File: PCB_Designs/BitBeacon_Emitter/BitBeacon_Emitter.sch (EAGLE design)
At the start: 9 parts, among them IC1 AD8607RM, IC2 AD8603UJ, Q1 TIP120

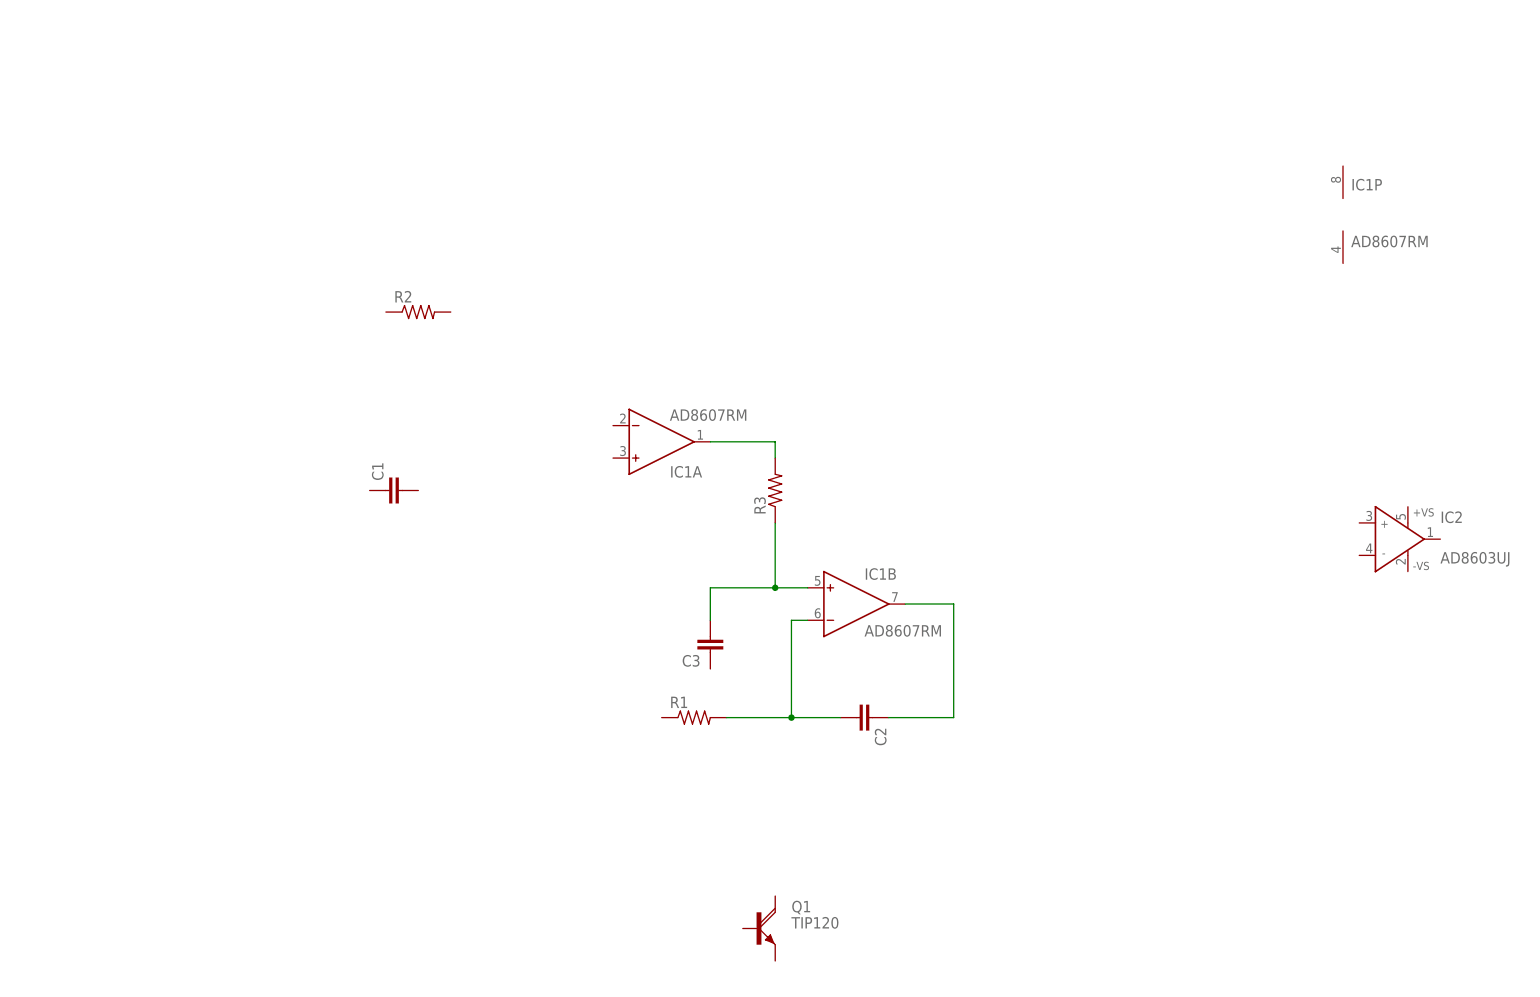
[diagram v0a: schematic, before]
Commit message: updating pcb files for emitter circuit
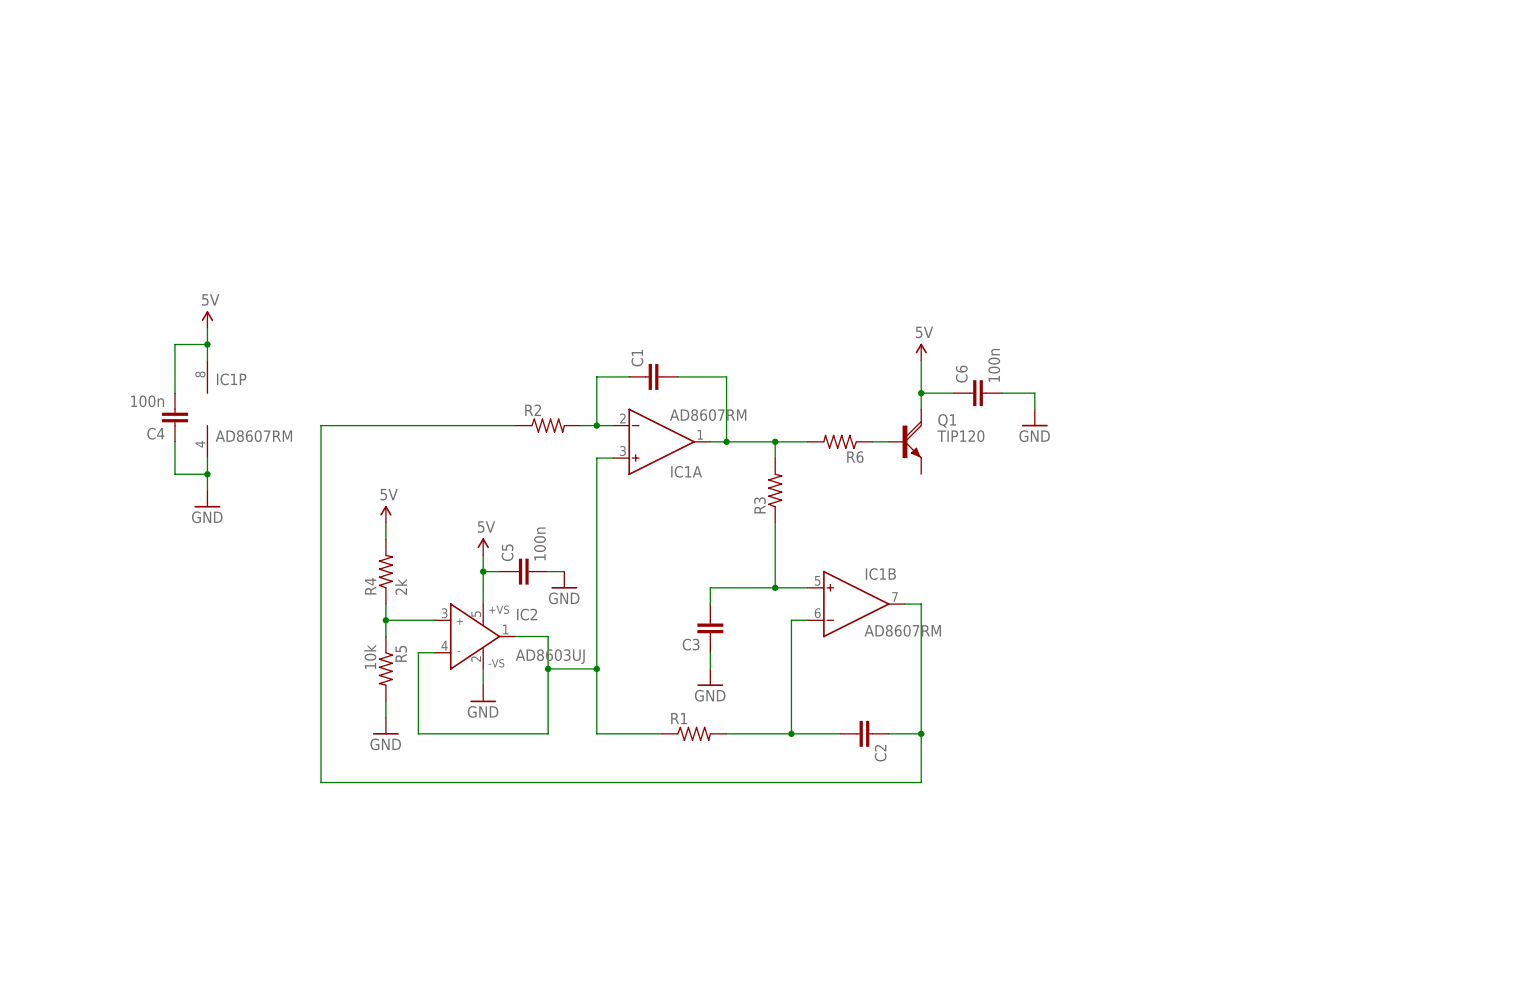
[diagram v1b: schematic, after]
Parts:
- added C4, C5, C6: 100n, resistor:C-EUC0402
- added R4: 2k, resistor:R-US_R0402
- added R5: 10k, resistor:R-US_R0402
- added R6: (no value), resistor:R-US_R0402
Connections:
- new net 5V: C4.2, C5.1, C6.1, IC1P.V+, IC2.+VS, Q1.C, R4.2
- new net GND: C3.1, C4.1, C5.2, C6.2, IC1P.V-, IC2.-VS, R5.2
- new net N$12: Q1.B, R6.1
- new net N$3: C1.1, IC1A.IN-, R2.2
- new net N$6: IC1A.IN+, IC2.IN-, IC2.OUT, R1.1
- new net N$7: IC2.IN+, R4.1, R5.1
- net N$1: now also C1.2, R6.2
- net N$4: now also R2.1
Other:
- moved on the sheet: C1, C2, C3, IC1P, IC2, Q1, R1, R2

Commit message: finished PCB design for Bit Beacon Emitter circuit and added datsheets for the LEDs that I think would work well.
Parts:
- removed Q1: TIP120, transistor-power:TIP120
- added JP1, JP2: M01NOSILK-KIT, SparkFun-Connectors:M01NOSILK-KIT
- added LED1, LED2, LED3: LED, Orlando:LED
- added LOGO1: OSHW-LOGOS, SparkFun-Aesthetics:OSHW-LOGOS
- added Q2: (no value), SparkFun-DiscreteSemi:TRANSISTOR_NPN2N3904
- added U$1: BATT-CONNECT, OrlandoRonMod:BATT-CONNECT
- C6: value 100n -> (none)
- R4: value 2k -> 5.1k
- renumbered IC1 to FGEN, IC2 to VREF
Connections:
- removed net N$1: C1.2, FGENA.OUT, R3.2, R6.2
- removed net N$12: Q1.B, R6.1
- removed net N$4: C2.1, FGENB.OUT, R2.1
- new net COSINE: C2.1, FGENB.OUT, JP2.1, R2.1
- new net N$8: LED1.C, LED2.C, LED3.C, Q2.C
- new net N$9: Q2.B, R6.1
- new net SINE: C1.2, FGENA.OUT, JP1.1, R3.2, R6.2
- net 5V: now also LED1.A, LED2.A, LED3.A, U$1G$2.TP; no longer Q1.C
- net GND: now also Q2.E, U$1G$1.TP
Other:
- note added: "Orlando S. Hoilett Bit Beacon Signal V.1.0 Calvary Eng, IICEPD Description: Sine wave generator circuit that drives a transistor to drive a few IR LEDs"
- note added: "Sources: Jean-Claude Wippler. "Generating a sine wave." <http://jeelabs.org/2012/05/18/generating-a-sine-wave/> Accessed: October 2015"
- moved on the sheet: C6, R6

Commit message: updated Bit emitter PCB design with resistor and capacitor values. Added a bill of materials for BitBeacon and BitBeacon_Emitter
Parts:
- C1, C2, C3: value (none) -> 1n
- C6: value (none) -> 100n
- R1, R2, R3: value (none) -> 22k
- R4: value 5.1k -> 22k
- R5: value 10k -> 22k
- R6: value (none) -> 100-400
- renumbered U$1 to BATTERY
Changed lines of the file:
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@@
 <?xml version="1.0" encoding="utf-8"?>
 <!DOCTYPE eagle SYSTEM "eagle.dtd">
-<eagle version="7.4.0">
+<eagle version="7.3.0">
 <drawing>
 <settings>
@@
 <part name="FGEN" library="analog-devices" deviceset="AD8607" device="RM" value=""/>
 <part name="VREF" library="analog-devices" deviceset="AD8603" device="UJ" value=""/>
-<part name="R1" library="resistor" deviceset="R-US_" device="R0402"/>
-<part name="R2" library="resistor" deviceset="R-US_" device="R0402"/>
-<part name="R3" library="resistor" deviceset="R-US_" device="R0402"/>
-<part name="C1" library="resistor" deviceset="C-EU" device="C0402"/>
-<part name="C2" library="resistor" deviceset="C-EU" device="C0402"/>
-<part name="C3" library="resistor" deviceset="C-EU" device="C0402"/>
+<part name="R1" library="resistor" deviceset="R-US_" device="R0402" value="22k"/>
+<part name="R2" library="resistor" deviceset="R-US_" device="R0402" value="22k"/>
+<part name="R3" library="resistor" deviceset="R-US_" device="R0402" value="22k"/>
+<part name="C1" library="resistor" deviceset="C-EU" device="C0402" value="1n"/>
+<part name="C2" library="resistor" deviceset="C-EU" device="C0402" value="1n"/>
+<part name="C3" library="resistor" deviceset="C-EU" device="C0402" value="1n"/>
 <part name="GND1" library="SparkFun-Aesthetics" deviceset="GND" device=""/>
-<part name="R4" library="resistor" deviceset="R-US_" device="R0402" value="5.1k"/>
-<part name="R5" library="resistor" deviceset="R-US_" device="R0402" value="10k"/>
+<part name="R4" library="resistor" deviceset="R-US_" device="R0402" value="22k"/>
+<part name="R5" library="resistor" deviceset="R-US_" device="R0402" value="22k"/>
 <part name="GND2" library="SparkFun-Aesthetics" deviceset="GND" device=""/>
 <part name="GND3" library="SparkFun-Aesthetics" deviceset="GND" device=""/>
@@
 <part name="C5" library="resistor" deviceset="C-EU" device="C0402" value="100n"/>
 <part name="GND5" library="SparkFun-Aesthetics" deviceset="GND" device=""/>
-<part name="R6" library="resistor" deviceset="R-US_" device="R0402"/>
+<part name="R6" library="resistor" deviceset="R-US_" device="R0402" value="100-400"/>
 <part name="SUPPLY4" library="SparkFun-Aesthetics" deviceset="5V" device=""/>
 <part name="LED1" library="Orlando" deviceset="LED" device=""/>
@@
 <part name="JP2" library="SparkFun-Connectors" deviceset="M01" device="NOSILK-KIT" value="M01NOSILK-KIT"/>
 <part name="LOGO1" library="SparkFun-Aesthetics" deviceset="OSHW-LOGO" device="S"/>
-<part name="U$1" library="OrlandoRonMod" deviceset="BATT-CONNECT" device=""/>
+<part name="BATTERY" library="OrlandoRonMod" deviceset="BATT-CONNECT" device=""/>
 <part name="SUPPLY5" library="SparkFun-Aesthetics" deviceset="5V" device=""/>
 <part name="GND7" library="SparkFun-Aesthetics" deviceset="GND" device=""/>
-<part name="C6" library="resistor" deviceset="C-EU" device="C0402"/>
+<part name="C6" library="resistor" deviceset="C-EU" device="C0402" value="100n"/>
 <part name="Q2" library="SparkFun-DiscreteSemi" deviceset="TRANSISTOR_NPN" device="2N3904"/>
 <part name="FRAME1" library="frames" deviceset="A4L-LOC" device=""/>
@@
 <instance part="JP2" gate="G$1" x="76.2" y="48.26" rot="R270"/>
 <instance part="LOGO1" gate="G$1" x="5.08" y="111.76"/>
-<instance part="U$1" gate="G$2" x="38.1" y="111.76"/>
-<instance part="U$1" gate="G$1" x="43.18" y="111.76"/>
+<instance part="BATTERY" gate="G$2" x="38.1" y="111.76"/>
+<instance part="BATTERY" gate="G$1" x="43.18" y="111.76"/>
 <instance part="SUPPLY5" gate="G$1" x="38.1" y="127"/>
 <instance part="GND7" gate="1" x="53.34" y="111.76"/>
@@
 </segment>
 <segment>
-<pinref part="U$1" gate="G$1" pin="TP"/>
+<pinref part="BATTERY" gate="G$1" pin="TP"/>
 <wire x1="43.18" y1="114.3" x2="43.18" y2="116.84" width="0.1524" layer="91"/>
 <wire x1="43.18" y1="116.84" x2="50.8" y2="116.84" width="0.1524" layer="91"/>
@@
 </segment>
 <segment>
-<pinref part="U$1" gate="G$2" pin="TP"/>
+<pinref part="BATTERY" gate="G$2" pin="TP"/>
 <wire x1="38.1" y1="114.3" x2="38.1" y2="121.92" width="0.1524" layer="91"/>
 <pinref part="SUPPLY5" gate="G$1" pin="5V"/>

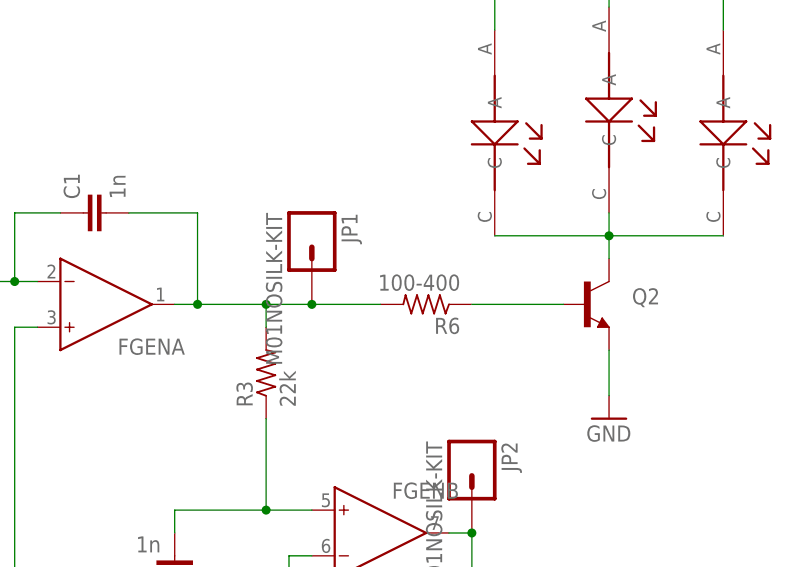
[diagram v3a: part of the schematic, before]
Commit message: updates to beacon emitter design
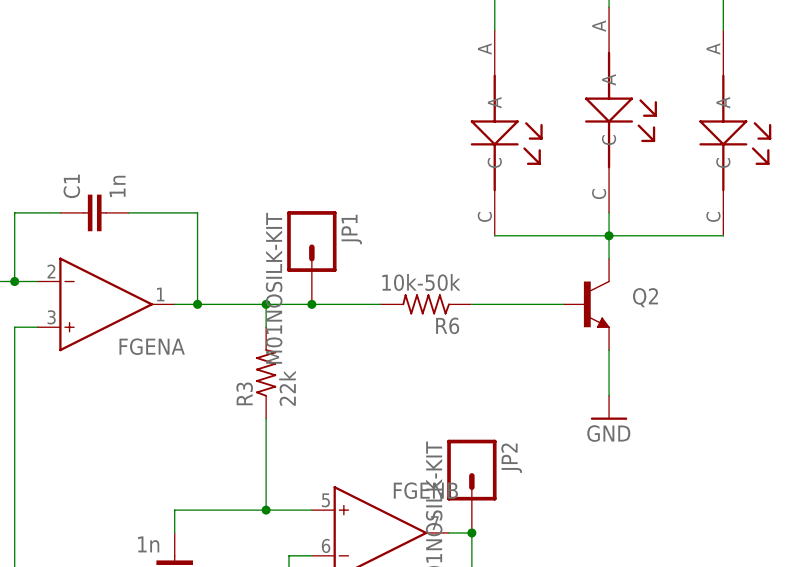
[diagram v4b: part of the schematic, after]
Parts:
- R6: value 100-400 -> 10k-50k
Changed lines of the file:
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@@
 <?xml version="1.0" encoding="utf-8"?>
 <!DOCTYPE eagle SYSTEM "eagle.dtd">
-<eagle version="7.3.0">
+<eagle version="7.4.0">
 <drawing>
 <settings>
@@
 <part name="C5" library="resistor" deviceset="C-EU" device="C0402" value="100n"/>
 <part name="GND5" library="SparkFun-Aesthetics" deviceset="GND" device=""/>
-<part name="R6" library="resistor" deviceset="R-US_" device="R0402" value="100-400"/>
+<part name="R6" library="resistor" deviceset="R-US_" device="R0402" value="10k-50k"/>
 <part name="SUPPLY4" library="SparkFun-Aesthetics" deviceset="5V" device=""/>
 <part name="LED1" library="Orlando" deviceset="LED" device=""/>
